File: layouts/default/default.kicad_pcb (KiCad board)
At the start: 2 copper layers, 11 parts

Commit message: finished PCB
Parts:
- added C6: 10µF ±10% 25V X5R, atopile:C0805-3b2e55, F.Cu at (80.4, 85.2)
- added C7: 100nF ±10% 16V X7R, atopile:C0402-b3ef17, F.Cu at (80.5, 86.8)
- added R4: 4.7kΩ ±1% 62.5mW, atopile:R0402-56259e, F.Cu at (79.1, 88.1)
- added R5: 4.7kΩ ±1% 62.5mW, atopile:R0402-56259e, F.Cu at (79.1, 91.1)
- added U4: , lib:WIRELM-SMD_ESP32-S3-WROOM-1, F.Cu at (86.6, 70.7)
- added U5: , lib:USB-C-SMD_KH-TYPE-C-16P, F.Cu at (74.8, 89.6)
- C1, C2, C5: value 100nF ±10% 16V X7R -> 10µF ±10% 25V X5R; footprint atopile:C0402-b3ef17 -> atopile:C0805-3b2e55
- C3, C4: value 10µF ±10% 25V X5R -> 100nF ±10% 16V X7R; footprint atopile:C0805-3b2e55 -> atopile:C0402-b3ef17
- R1, R2: value 1kΩ ±1% 62.5mW -> 10kΩ ±1% 62.5mW
- U1: footprint atopile:LGA-8_L3.0-W3.0-P0.80_BME688-7465bb -> lib:SOT-223-3_L6.5-W3.4-P2.30-LS7.0-BR
- U2: footprint lib:KEY-SMD_4P-L4.2-W3.2-P2.20-LS4.6 -> atopile:LGA-8_L3.0-W3.0-P0.80_BME688-7465bb
- U3: footprint lib:WIRELM-SMD_ESP32-S3-WROOM-1 -> lib:KEY-SMD_4P-L4.2-W3.2-P2.20-LS4.6
- moved C2 157.4 mm to (83.0, 93.7), turned to 180 degrees
- moved U1 148.6 mm to (86.8, 90.6)
- moved C5 137.2 mm to (92.6, 89.5), turned to -90 degrees
- moved R2 131.5 mm to (91.9, 84.1), turned to 90 degrees
- moved C1 130.7 mm to (80.4, 83.1)
- moved U3 128.9 mm to (73.2, 82.3)
- moved R1 125.5 mm to (93.2, 84.1), turned to 90 degrees
- moved C4 115.4 mm to (80.3, 81.5)
- moved C3 113.0 mm to (85.8, 83.8), turned to -90 degrees
- moved U2 102.6 mm to (88.8, 84.1)
- moved R3 100.2 mm to (77.2, 82.3), turned to 180 degrees
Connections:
- C2 pad 1: hv -> hv-1
- R1 pad 2: CSB -> VDDIO
- R2 pad 2: CSB -> VDDIO
- U1 pad 2: CSB -> hv-1
- U1 pad 3: SDI -> hv
- U1 pad 4: SCK -> hv-1
- U2 pad 1: in -> gnd
- U2 pad 2: in -> VDDIO
- U2 pad 3: gnd -> SDI
- U2 pad 4: gnd -> SCK
- U3 pad 1: gnd -> in
- U3 pad 2: hv -> in
- U3 pad 3: EN -> gnd
- U3 pad 4: io4 -> gnd
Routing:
- net gnd: track 0.00 -> 65.0 mm, vias 0 -> 12
- net hv: track 0.00 -> 49.2 mm, vias 0 -> 2
- net io20: track 0.00 -> 26.0 mm, vias 0 -> 2
- net io19: track 0.00 -> 24.1 mm, vias 0 -> 2
- net SDI: track 0.00 -> 22.3 mm
- net SCK: track 0.00 -> 17.7 mm
- net EN: track 0.00 -> 16.4 mm, vias 0 -> 2
- net hv-1: track 0.00 -> 9.14 mm
- net VDDIO: track 0.00 -> 6.16 mm
- net A5: track 0.00 -> 1.62 mm
- net CC2: track 0.00 -> 1.56 mm
- added copper zone on B.Cu, net gnd
- added copper zone on F.Cu, net gnd
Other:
- board outline added: 27.1 x 34.7 mm
- board text added: "04/25 NonHumanScent eigenlucy/nonhumanscent"

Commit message: finished PCB
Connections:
- net A8 renamed SUB1
- net SUB2 renamed B8
- net VDDIO renamed CSB
- U4 pad : (no net) -> gnd
- U4 pad 3: EN -> in
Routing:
- net in: track 0.00 -> 16.7 mm, vias 0 -> 2
- net EN: track 16.4 -> 0.00 mm, vias 2 -> 0
- net gnd: track 65.0 -> 80.3 mm

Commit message: changed main build to app to fix build action
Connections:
- net A5 renamed CC1
- net CC2 renamed B5
- net SUB1 renamed A8
- C1 pad 1: hv -> hv-1
- C2 pad 1: hv-1 -> hv
- C3 pad 1: hv -> hv-1
- C4 pad 1: hv -> hv-1
- C5 pad 1: hv -> hv-1
- C6 pad 1: hv -> hv-1
- C7 pad 1: hv -> hv-1
- R3 pad 1: hv -> hv-1
- U1 pad 2: hv-1 -> hv
- U1 pad 3: hv -> hv-1
- U1 pad 4: hv-1 -> hv
- U2 pad 8: hv -> hv-1
- U4 pad 2: hv -> hv-1
- U5 pad A4: hv -> hv-1
- U5 pad A9: hv -> hv-1
- U5 pad B4: hv -> hv-1
- U5 pad B9: hv -> hv-1
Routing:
- net hv-1: track 9.14 -> 49.2 mm, vias 0 -> 2
- net hv: track 49.2 -> 9.14 mm, vias 2 -> 0
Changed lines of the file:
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@@
     (net 3 "io45")
     (net 4 "io37")
-    (net 5 "CC2")
+    (net 5 "B5")
     (net 6 "SDI")
     (net 7 "io16")
@@
     (net 33 "CSB")
     (net 34 "io3")
-    (net 35 "SUB1")
-    (net 36 "A5")
-    (net 37 "hv")
+    (net 35 "A8")
+    (net 36 "CC1")
+    (net 37 "hv-1")
     (net 38 "io15")
     (net 39 "io21")
@@
     (net 43 "gnd")
     (net 44 "io35")
-    (net 45 "hv-1")
+    (net 45 "hv")
     (net 46 "in")
     (footprint "atopile:C0402-b3ef17"
@@
             (size 0.79 0.54)
             (layers "F.Cu" "F.Mask" "F.Paste")
-            (net 37 "hv")
+            (net 37 "hv-1")
         )
         (pad "2" smd rect
@@
             (size 2.5 1.1)
             (layers "F.Cu" "F.Mask" "F.Paste")
-            (net 45 "hv-1")
+            (net 45 "hv")
         )
         (pad "3" smd rect
@@
             (size 2.5 1.1)
             (layers "F.Cu" "F.Mask" "F.Paste")
-            (net 37 "hv")
+            (net 37 "hv-1")
         )
         (pad "4" smd rect
@@
             (size 2.34 3.6)
             (layers "F.Cu" "F.Mask" "F.Paste")
-            (net 45 "hv-1")
+            (net 45 "hv")
         )
         (embedded_fonts no)
@@
             (size 0.57 0.54)
             (layers "F.Cu" "F.Mask" "F.Paste")
-            (net 5 "CC2")
+            (net 5 "B5")
         )
         (pad "2" smd rect
@@
             (size 1.41 1.35)
             (layers "F.Cu" "F.Mask" "F.Paste")
-            (net 37 "hv")
+            (net 37 "hv-1")
         )
         (pad "2" smd rect
@@
             (size 1.5 0.9)
             (layers "F.Cu" "F.Mask" "F.Paste")
-            (net 37 "hv")
+            (net 37 "hv-1")
         )
         (pad "3" smd rect
@@
             (size 1.41 1.35)
             (layers "F.Cu" "F.Mask" "F.Paste")
-            (net 45 "hv-1")
+            (net 45 "hv")
         )
         (pad "2" smd rect
@@
             (size 0.79 0.54)
             (layers "F.Cu" "F.Mask" "F.Paste")
-            (net 37 "hv")
+            (net 37 "hv-1")
         )
         (pad "2" smd rect
@@
             (size 0.3 1.3)
             (layers "F.Cu" "F.Mask" "F.Paste")
-            (net 37 "hv")
+            (net 37 "hv-1")
         )
         (pad "A5" smd rect
@@
             (size 0.3 1.3)
             (layers "F.Cu" "F.Mask" "F.Paste")
-            (net 36 "A5")
+            (net 36 "CC1")
         )
         (pad "A6" smd rect
@@
             (size 0.3 1.3)
             (layers "F.Cu" "F.Mask" "F.Paste")
-            (net 35 "SUB1")
+            (net 35 "A8")
         )
         (pad "A9" smd rect
@@
             (size 0.3 1.3)
             (layers "F.Cu" "F.Mask" "F.Paste")
-            (net 37 "hv")
+            (net 37 "hv-1")
         )
         (pad "A12" smd rect
@@
             (size 0.3 1.3)
             (layers "F.Cu" "F.Mask" "F.Paste")
-            (net 37 "hv")
+            (net 37 "hv-1")
         )
         (pad "B5" smd rect
@@
             (size 0.3 1.3)
             (layers "F.Cu" "F.Mask" "F.Paste")
-            (net 5 "CC2")
+            (net 5 "B5")
         )
         (pad "B6" smd rect
@@
             (size 0.3 1.3)
             (layers "F.Cu" "F.Mask" "F.Paste")
-            (net 37 "hv")
+            (net 37 "hv-1")
         )
         (pad "B12" smd rect
@@
             (size 0.57 0.54)
             (layers "F.Cu" "F.Mask" "F.Paste")
-            (net 37 "hv")
+            (net 37 "hv-1")
         )
         (pad "2" smd rect
@@
             (size 1.41 1.35)
             (layers "F.Cu" "F.Mask" "F.Paste")
-            (net 37 "hv")
+            (net 37 "hv-1")
         )
         (pad "2" smd rect
@@
             (size 0.57 0.54)
             (layers "F.Cu" "F.Mask" "F.Paste")
-            (net 36 "A5")
+            (net 36 "CC1")
         )
         (pad "2" smd rect
@@
             (size 0.45 0.89)
             (layers "F.Cu" "F.Mask" "F.Paste")
-            (net 37 "hv")
+            (net 37 "hv-1")
         )
         (embedded_fonts no)
@@
             (size 1.41 1.35)
             (layers "F.Cu" "F.Mask" "F.Paste")
-            (net 37 "hv")
+            (net 37 "hv-1")
         )
         (pad "2" smd rect
@@
             (size 0.79 0.54)
             (layers "F.Cu" "F.Mask" "F.Paste")
-            (net 37 "hv")
+            (net 37 "hv-1")
         )
         (pad "2" smd rect

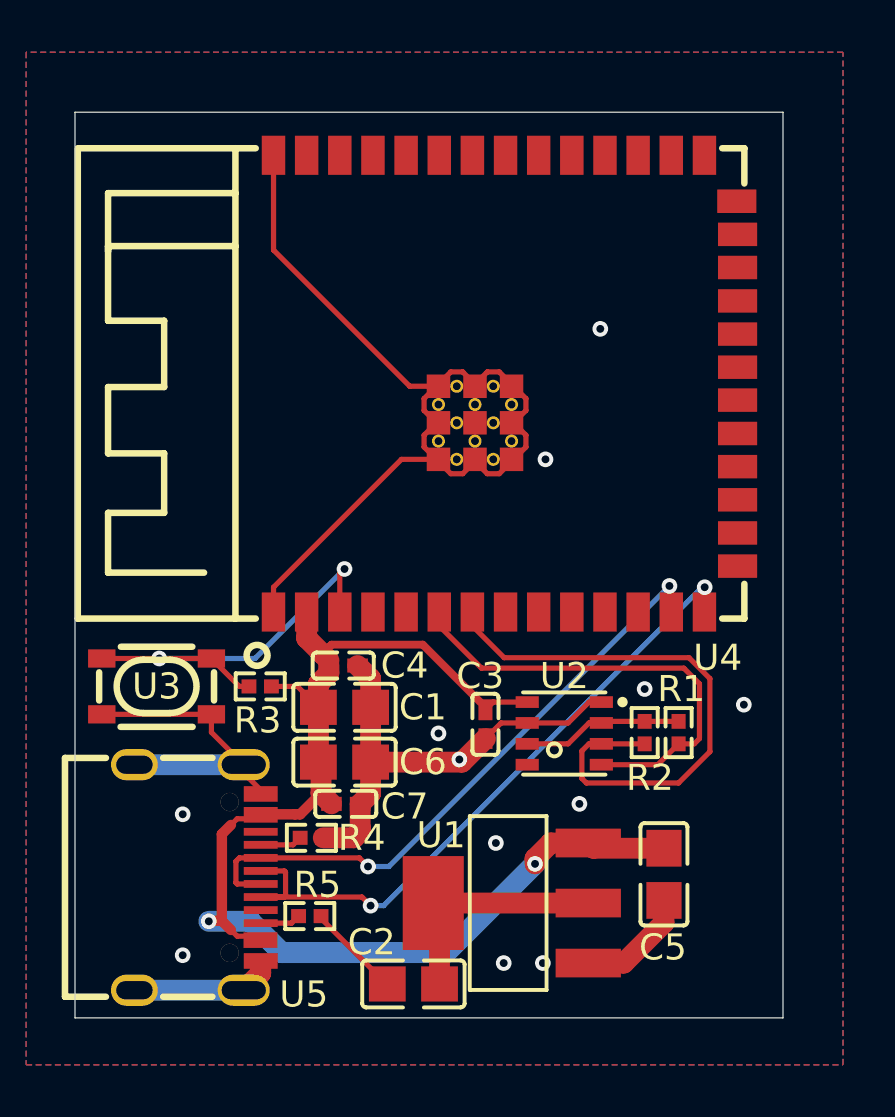
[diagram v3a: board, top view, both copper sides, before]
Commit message: fixed power rails and added sd card
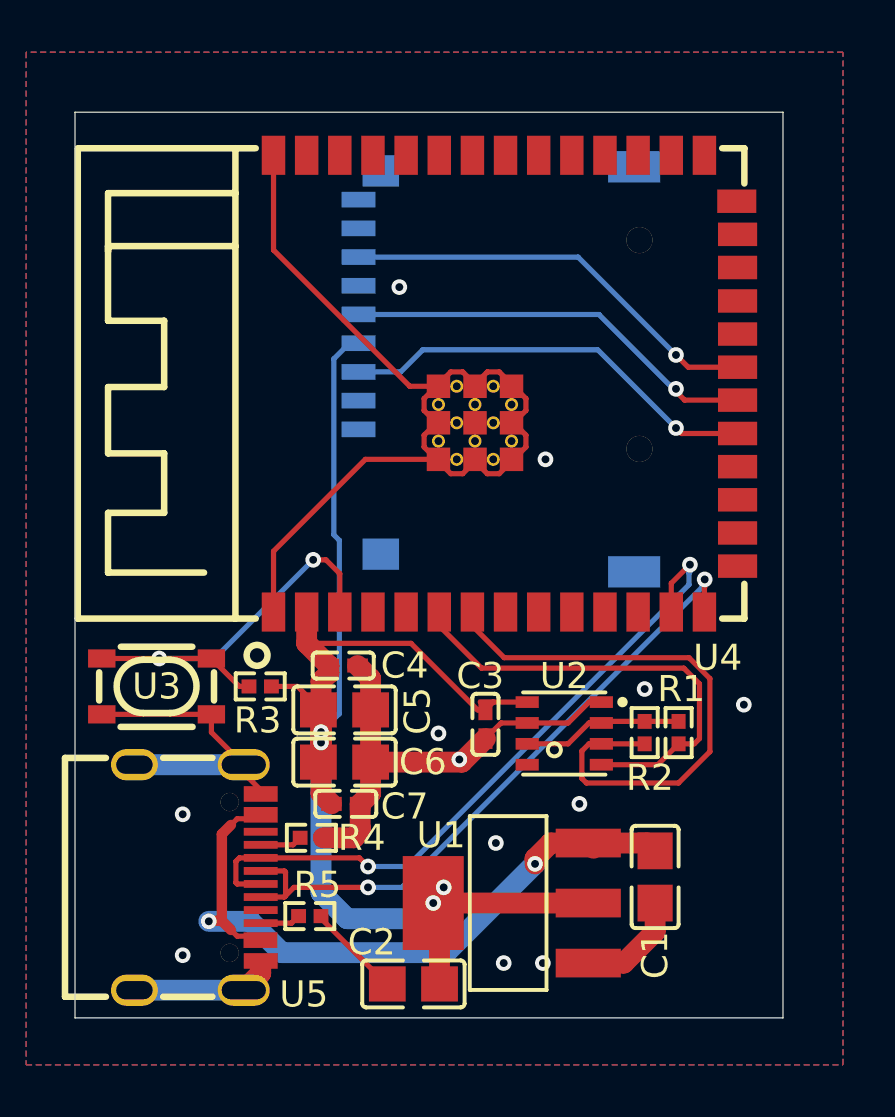
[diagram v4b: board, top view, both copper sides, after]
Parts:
- added U6: , lib:TF-SMD_TF-01A, B.Cu at (86.2, 70.2)
- R1, R2: value 10kΩ ±1% 62.5mW -> 1kΩ ±1% 62.5mW
- moved C5 13.8 mm to (80.4, 83.2), turned to 0 degrees
- moved C1 13.6 mm to (92.3, 89.6), turned to -90 degrees
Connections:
- C1 pad 1: hv-1 -> hv
- C2 pad 1: hv -> hv-1
- U1 pad 2: hv -> hv-1
- U1 pad 3: hv-1 -> hv
- U1 pad 4: hv -> hv-1
- U4 pad 19: io11 -> CMD_DI_
- U4 pad 20: io12 -> CLK_SCLK_
- U4 pad 21: io13 -> DAT0_D0_
- U5 pad A4: hv-1 -> hv
- U5 pad A9: hv-1 -> hv
- U5 pad B4: hv-1 -> hv
- U5 pad B9: hv-1 -> hv
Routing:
- net hv: track 9.14 -> 27.3 mm, vias 0 -> 2
- net DAT0_D0_: track 0.00 -> 16.3 mm, vias 0 -> 1
- net CMD_DI_: track 0.00 -> 16.2 mm, vias 0 -> 1
- net CLK_SCLK_: track 0.00 -> 15.9 mm, vias 0 -> 1
- net hv-1: track 49.2 -> 58.6 mm, vias 2 -> 4
- net io19: track 24.1 -> 26.7 mm
- net gnd: track 80.3 -> 81.1 mm
- net io20: track 26.0 -> 25.3 mm
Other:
- board text added: "04/25/25 NonHumanScent"
- board text added: "eigenlucy/nonhumanscent"
- board text removed: "04/25 NonHumanScent eigenlucy/nonhumanscent"

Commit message: --no-frozen
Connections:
- net B5 renamed CC2
- net B8 renamed SUB2
- net CC1 renamed A5
- C1 pad 1: hv -> hv-1
- C2 pad 1: hv-1 -> hv
- C3 pad 1: hv-1 -> hv
- C4 pad 1: hv-1 -> hv
- C5 pad 1: hv-1 -> hv
- C6 pad 1: hv-1 -> hv
- C7 pad 1: hv-1 -> hv
- R3 pad 1: hv-1 -> hv
- U1 pad 2: hv-1 -> hv
- U1 pad 3: hv -> hv-1
- U1 pad 4: hv-1 -> hv
- U2 pad 8: hv-1 -> hv
- U4 pad 2: hv-1 -> hv
- U5 pad A4: hv -> hv-1
- U5 pad A9: hv -> hv-1
- U5 pad B4: hv -> hv-1
- U5 pad B9: hv -> hv-1
- U6 pad 4: hv-1 -> hv
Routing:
- net hv-1: track 58.6 -> 27.3 mm, vias 4 -> 2
- net hv: track 27.3 -> 58.6 mm, vias 2 -> 4
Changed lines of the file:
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@@
     (net 3 "io45")
     (net 4 "io37")
-    (net 5 "B5")
+    (net 5 "CC2")
     (net 6 "SDI")
     (net 7 "io16")
@@
     (net 9 "io36")
     (net 10 "io1")
-    (net 11 "B8")
+    (net 11 "SUB2")
     (net 12 "io46")
     (net 13 "io20")
@@
     (net 31 "io3")
     (net 32 "A8")
-    (net 33 "CC1")
-    (net 34 "hv")
+    (net 33 "A5")
+    (net 34 "hv-1")
     (net 35 "io15")
     (net 36 "io21")
@@
     (net 48 "DAT0_D0_")
     (net 49 "CMD_DI_")
-    (net 50 "hv-1")
+    (net 50 "hv")
     (footprint "atopile:C0402-b3ef17"
         (layer "F.Cu")
@@
             (size 0.79 0.54)
             (layers "F.Cu" "F.Mask" "F.Paste")
-            (net 50 "hv-1")
+            (net 50 "hv")
         )
         (pad "2" smd rect
@@
             (size 2.5 1.1)
             (layers "F.Cu" "F.Mask" "F.Paste")
-            (net 50 "hv-1")
+            (net 50 "hv")
         )
         (pad "3" smd rect
@@
             (size 2.5 1.1)
             (layers "F.Cu" "F.Mask" "F.Paste")
-            (net 34 "hv")
+            (net 34 "hv-1")
         )
         (pad "4" smd rect
@@
             (size 2.34 3.6)
             (layers "F.Cu" "F.Mask" "F.Paste")
-            (net 50 "hv-1")
+            (net 50 "hv")
         )
         (embedded_fonts no)
@@
             (size 0.57 0.54)
             (layers "F.Cu" "F.Mask" "F.Paste")
-            (net 5 "B5")
+            (net 5 "CC2")
         )
         (pad "2" smd rect
@@
             (size 1.41 1.35)
             (layers "F.Cu" "F.Mask" "F.Paste")
-            (net 34 "hv")
+            (net 34 "hv-1")
         )
         (pad "2" smd rect
@@
             (size 1.5 0.9)
             (layers "F.Cu" "F.Mask" "F.Paste")
-            (net 50 "hv-1")
+            (net 50 "hv")
         )
         (pad "3" smd rect
@@
             (size 1.41 1.35)
             (layers "F.Cu" "F.Mask" "F.Paste")
-            (net 50 "hv-1")
+            (net 50 "hv")
         )
         (pad "2" smd rect
@@
             (size 0.79 0.54)
             (layers "F.Cu" "F.Mask" "F.Paste")
-            (net 50 "hv-1")
+            (net 50 "hv")
         )
         (pad "2" smd rect
@@
             (size 0.3 1.3)
             (layers "F.Cu" "F.Mask" "F.Paste")
-            (net 34 "hv")
+            (net 34 "hv-1")
         )
         (pad "A5" smd rect
@@
             (size 0.3 1.3)
             (layers "F.Cu" "F.Mask" "F.Paste")
-            (net 33 "CC1")
+            (net 33 "A5")
         )
         (pad "A6" smd rect
@@
             (size 0.3 1.3)
             (layers "F.Cu" "F.Mask" "F.Paste")
-            (net 34 "hv")
+            (net 34 "hv-1")
         )
         (pad "A12" smd rect
@@
             (size 0.3 1.3)
             (layers "F.Cu" "F.Mask" "F.Paste")
-            (net 34 "hv")
+            (net 34 "hv-1")
         )
         (pad "B5" smd rect
@@
             (size 0.3 1.3)
             (layers "F.Cu" "F.Mask" "F.Paste")
-            (net 5 "B5")
+            (net 5 "CC2")
         )
         (pad "B6" smd rect
@@
             (size 0.3 1.3)
             (layers "F.Cu" "F.Mask" "F.Paste")
-            (net 11 "B8")
+            (net 11 "SUB2")
         )
         (pad "B9" smd rect
@@
             (size 0.3 1.3)
             (layers "F.Cu" "F.Mask" "F.Paste")
-            (net 34 "hv")
+            (net 34 "hv-1")
         )
         (pad "B12" smd rect
@@
             (size 0.57 0.54)
             (layers "F.Cu" "F.Mask" "F.Paste")
-            (net 50 "hv-1")
+            (net 50 "hv")
         )
         (pad "2" smd rect
@@
             (size 1.41 1.35)
             (layers "F.Cu" "F.Mask" "F.Paste")
-            (net 50 "hv-1")
+            (net 50 "hv")
         )
         (pad "2" smd rect
@@
             (size 0.57 0.54)
             (layers "F.Cu" "F.Mask" "F.Paste")
-            (net 33 "CC1")
+            (net 33 "A5")
         )
         (pad "2" smd rect
@@
             (size 0.45 0.89)
             (layers "F.Cu" "F.Mask" "F.Paste")
-            (net 50 "hv-1")
+            (net 50 "hv")
         )
         (embedded_fonts no)
@@
             (size 1.41 1.35)
             (layers "F.Cu" "F.Mask" "F.Paste")
-            (net 50 "hv-1")
+            (net 50 "hv")
         )
         (pad "2" smd rect
@@
             (size 0.79 0.54)
             (layers "F.Cu" "F.Mask" "F.Paste")
-            (net 50 "hv-1")
+            (net 50 "hv")
         )
         (pad "2" smd rect
@@
             (size 0.6 1.3)
             (layers "B.Cu" "B.Mask" "B.Paste")
-            (net 50 "hv-1")
+            (net 50 "hv")
         )
         (pad "5" smd rect
